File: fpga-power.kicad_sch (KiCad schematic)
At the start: 100 parts, among them U3002 XC7K160T-FFG676

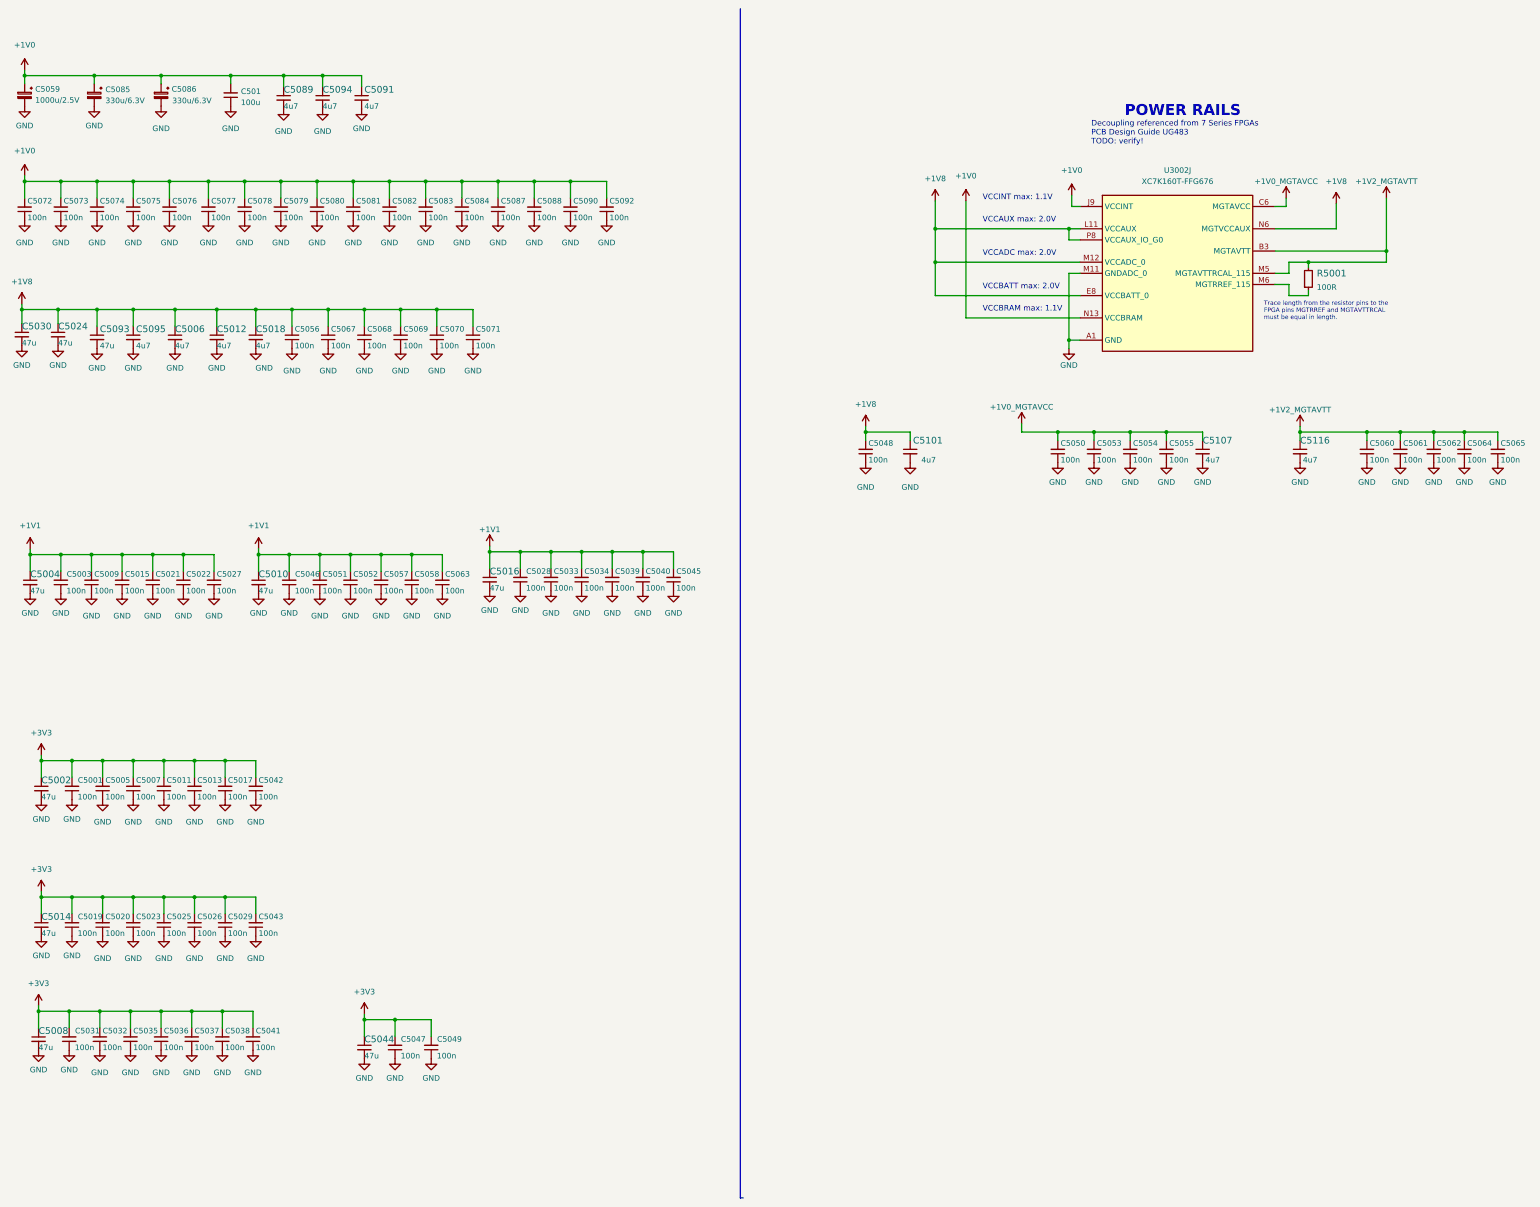
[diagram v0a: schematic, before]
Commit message: Re-annotate schematic
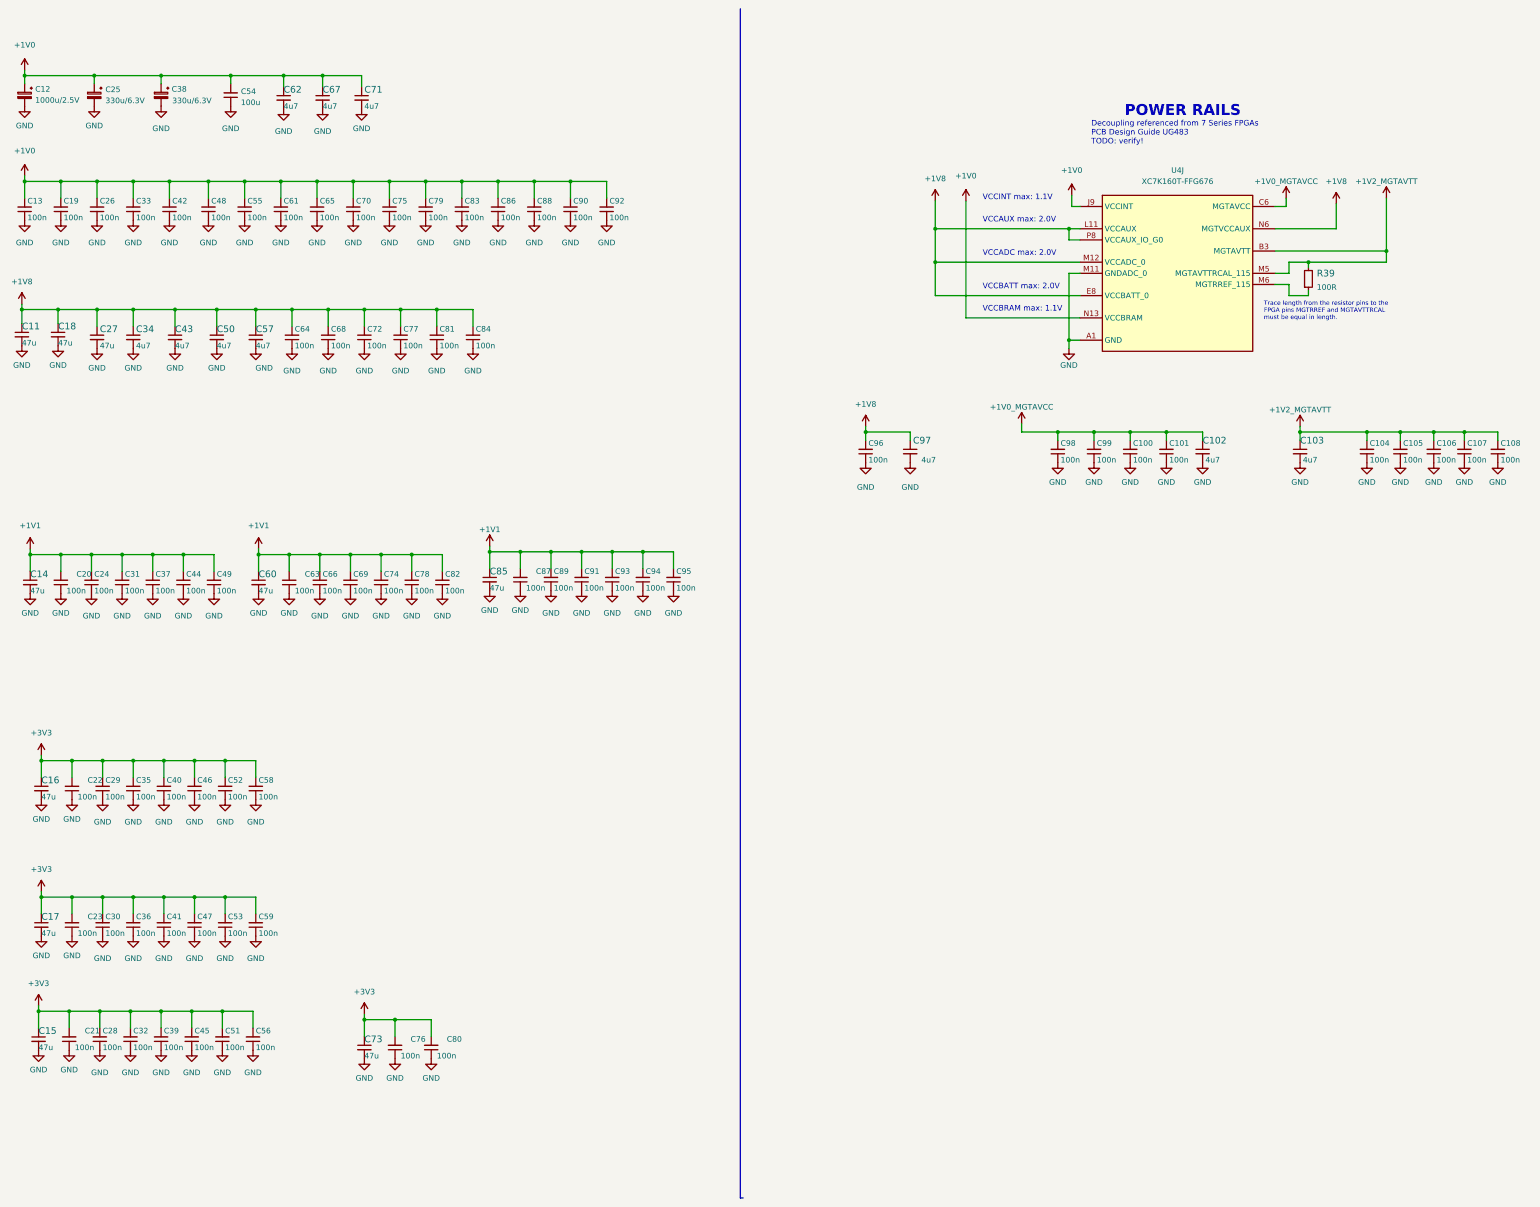
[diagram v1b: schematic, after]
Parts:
- renumbered C5054 to C100, C5055 to C101, C5107 to C102, C5116 to C103, C5060 to C104, C5061 to C105, C5062 to C106, C5064 to C107, C5065 to C108, C5030 to C11, C5059 to C12, C5072 to C13, C5004 to C14, C5008 to C15, C5002 to C16, C5014 to C17, C5024 to C18, C5073 to C19, C5003 to C20, C5031 to C21, C5001 to C22, C5019 to C23, C5009 to C24, C5085 to C25, C5074 to C26, C5093 to C27, C5032 to C28, C5005 to C29, C5020 to C30, C5015 to C31, C5035 to C32, C5075 to C33, C5095 to C34, C5007 to C35, C5023 to C36, C5021 to C37, C5086 to C38, C5036 to C39, C5011 to C40, C5025 to C41, C5076 to C42, C5006 to C43, C5022 to C44, C5037 to C45, C5013 to C46, C5026 to C47, C5077 to C48, C5027 to C49, C5012 to C50, C5038 to C51, C5017 to C52, C5029 to C53, C501 to C54, C5078 to C55, C5041 to C56, C5018 to C57, C5042 to C58, C5043 to C59, C5010 to C60, C5079 to C61, C5089 to C62, C5046 to C63, C5056 to C64, C5080 to C65, C5051 to C66, C5094 to C67, C5067 to C68, C5052 to C69, C5081 to C70, C5091 to C71, C5068 to C72, C5044 to C73, C5057 to C74, C5082 to C75, C5047 to C76, C5069 to C77, C5058 to C78, C5083 to C79, C5049 to C80, C5070 to C81, C5063 to C82, C5084 to C83, C5071 to C84, C5016 to C85, C5087 to C86, C5028 to C87, C5088 to C88, C5033 to C89, C5090 to C90, C5034 to C91, C5092 to C92, C5039 to C93, C5040 to C94, C5045 to C95, C5048 to C96, C5101 to C97, C5050 to C98, C5053 to C99, R5001 to R39, U3002 to U4

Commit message: Add local libraries
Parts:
- C12: footprint antmicro-footprints:C_Pol_EIA-D -> sodimm-ddr5-tester-footprints:C_Pol_EIA-D; symbol antmicroCapacitorspol:C_Pol_1m_2.5V_KEMET-T520-D -> sodimm-ddr5-tester:C_Pol_1m_2.5V_KEMET-T520-D
- C25, C38: footprint antmicro-footprints:C_Pol_EIA-B -> sodimm-ddr5-tester-footprints:C_Pol_EIA-B; symbol antmicroCapacitorspol:C_Pol_330u_6.3V_KEMET-T520-B -> sodimm-ddr5-tester:C_Pol_330u_6.3V_KEMET-T520-B

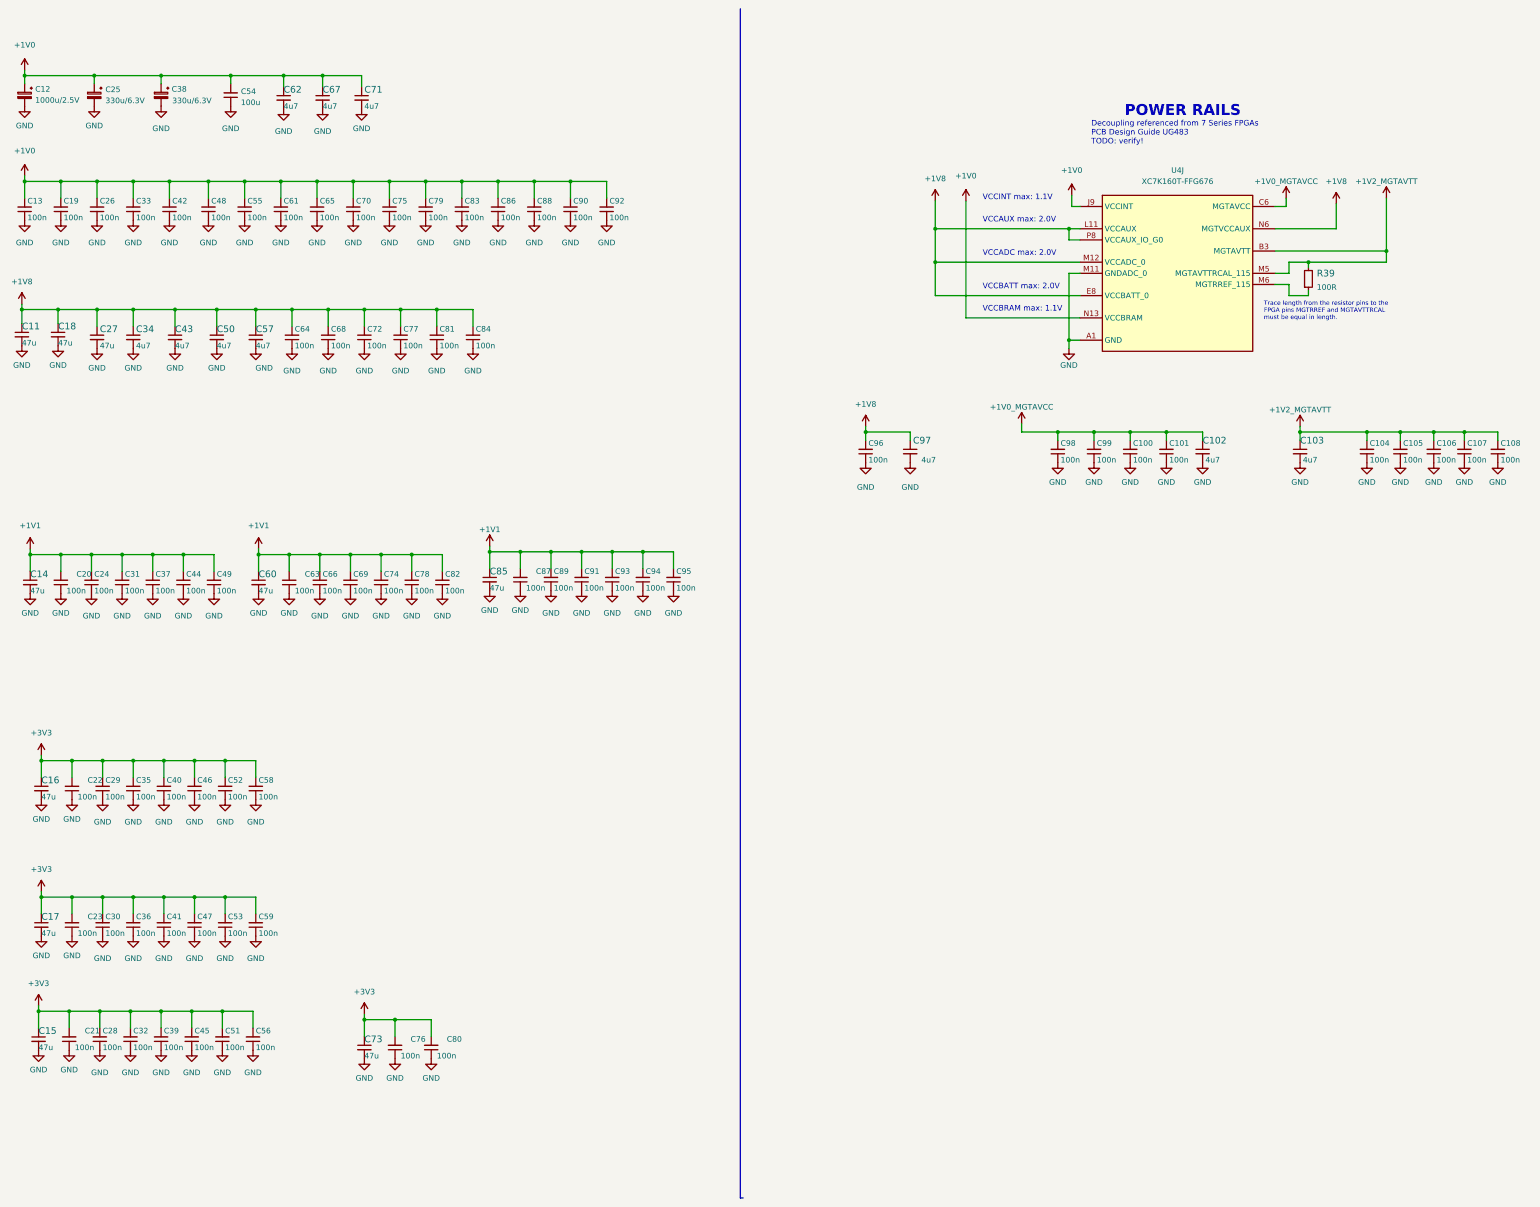
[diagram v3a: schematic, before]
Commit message: Connect DDR hierarchical labels. Define and connect JTAG, RGMII, TDMS, UART, and SDIO buses. Reorganize schematic blocks between sheets
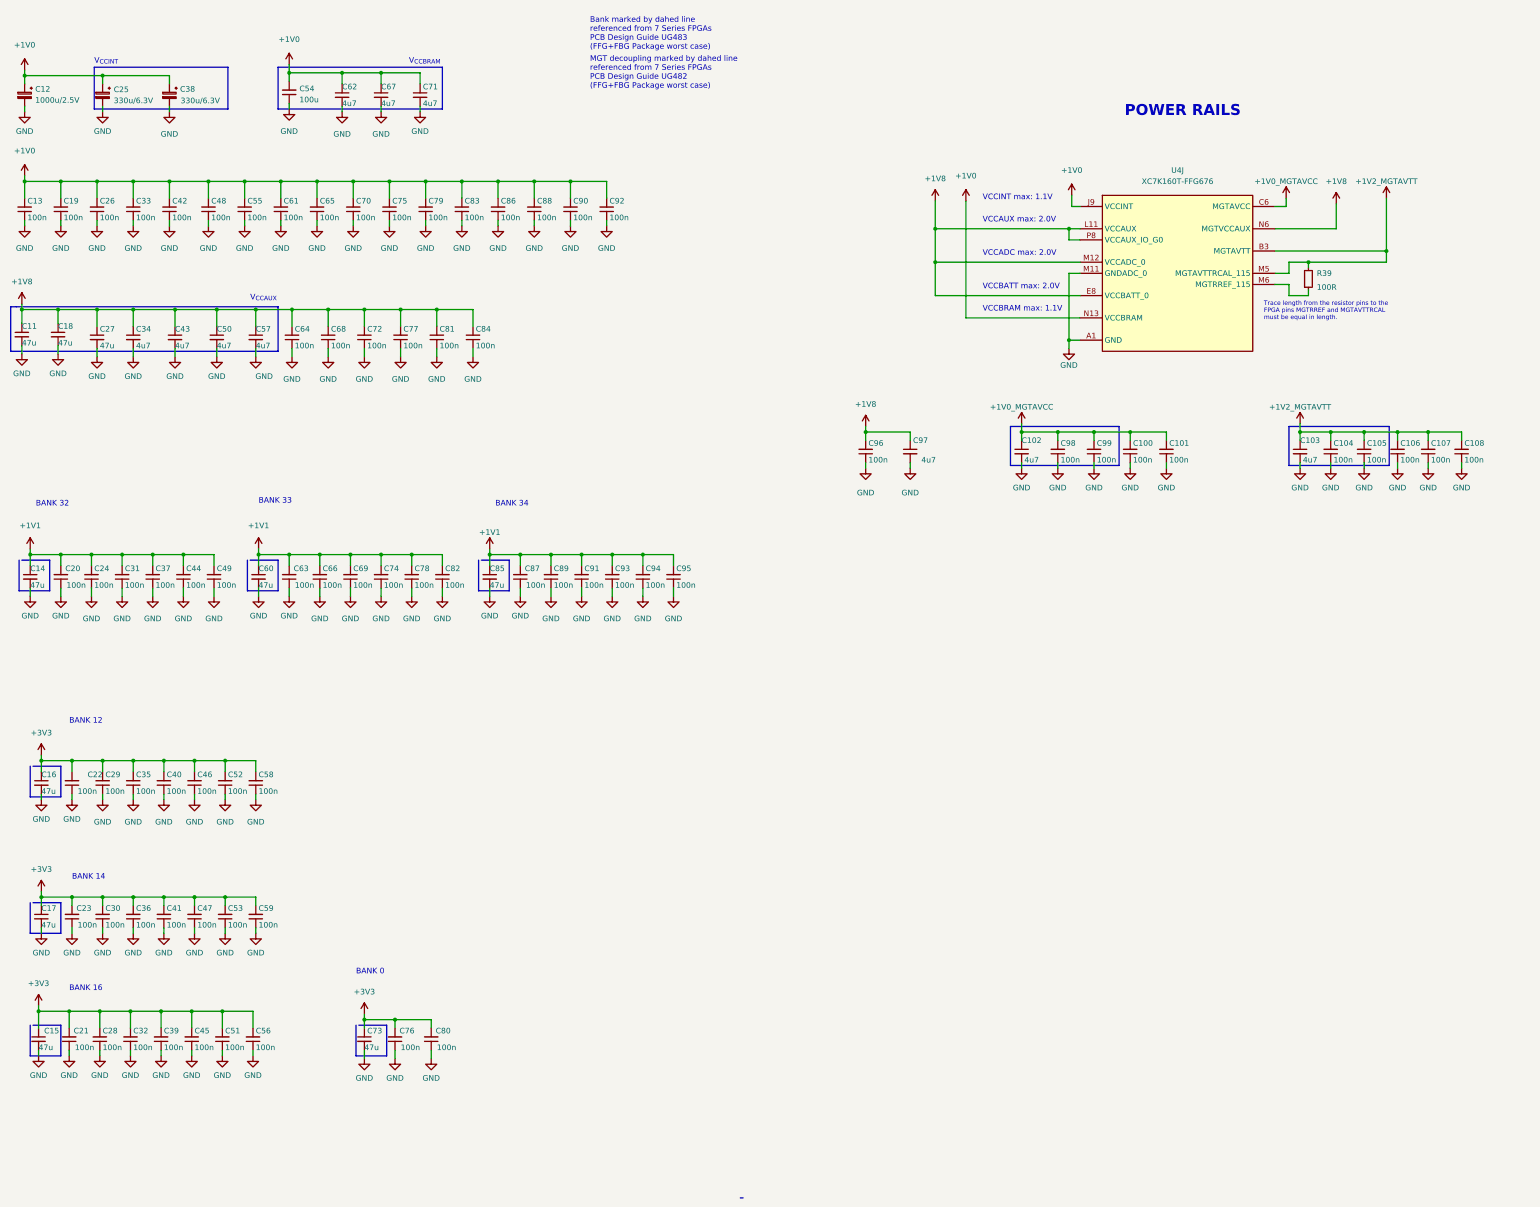
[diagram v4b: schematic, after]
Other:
- note added: "BANK 0"
- note added: "BANK 12"
- note added: "BANK 14"
- note added: "BANK 16"
- note added: "BANK 32"
- note added: "BANK 33"
- note added: "BANK 34"
- note added: "Bank marked by dahed line referenced from 7 Series FPGAs PCB Design Guide UG483 (FFG+FBG Package worst case)"
- note added: "MGT decoupling marked by dahed line referenced from 7 Series FPGAs PCB Design Guide UG482 (FFG+FBG Package worst case)"
- note added: "V_{CCAUX}"
- note added: "V_{CCBRAM}"
- note added: "V_{CCINT}"
- note removed: "Decoupling referenced from 7 Series FPGAs PCB Design Guide UG483 TODO: verify!"
- moved on the sheet: C102, C104, C105, C106, C107, C108, C14, C16, C17, C20, C22, C23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

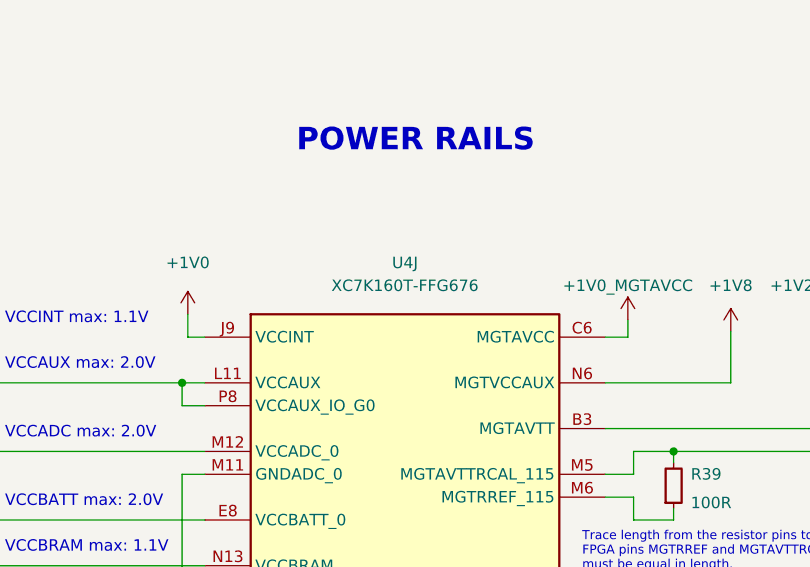
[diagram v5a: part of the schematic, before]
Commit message: Fix FPGA properties from the standardized library, update SO-DIMM symbol
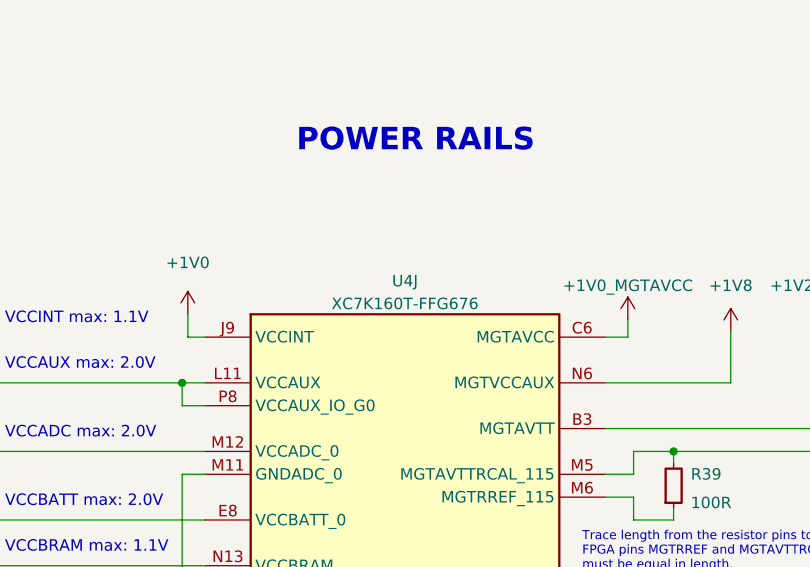
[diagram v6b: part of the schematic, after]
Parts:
- U4: footprint sodimm-ddr5-tester-footprints:BGA-676_27x27mm_Layout26x26_P1X1mm -> antmicro-footprints:BGA-676_27x27mm_Layout26x26_P1X1mm; symbol sodimm-ddr5-tester:XC7K160T-FFG676 -> antmicroMicrocontrollers:XC7K160T-FFG676; Manufacturer Xilinx -> AMD-Xilinx
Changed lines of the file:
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@@
     (pin "1")
   )
-  (symbol (lib_id "sodimm-ddr5-tester:XC7K160T-FFG676") (at 268.605 57.785 0) (unit 10)
+  (symbol (lib_id "antmicroMicrocontrollers:XC7K160T-FFG676") (at 268.605 57.785 0) (unit 10)
     (in_bom yes) (on_board yes) (fields_autoplaced)
-    (property "Reference" "U4" (id 0) (at 290.83 49.53 0))
-    (property "Value" "XC7K160T-FFG676" (id 1) (at 290.83 52.07 0)
+    (property "Reference" "U4" (id 0) (at 290.83 51.5534 0))
+    (property "Value" "XC7K160T-FFG676" (id 1) (at 290.83 54.0837 0)
       (effects (font (size 1.27 1.27) (thickness 0.15)))
     )
-    (property "Footprint" "sodimm-ddr5-tester-footprints:BGA-676_27x27mm_Layout26x26_P1X1mm" (id 2) (at 337.185 60.325 0)
+    (property "Footprint" "antmicro-footprints:BGA-676_27x27mm_Layout26x26_P1X1mm" (id 2) (at 337.185 60.325 0)
       (effects (font (size 1.27 1.27) (thickness 0.15)) (justify left bottom) hide)
     )
@@
       (effects (font (size 1.27 1.27) (thickness 0.15)) (justify left bottom) hide)
     )
-    (property "Manufacturer" "Xilinx" (id 7) (at 268.605 57.785 0)
+    (property "Manufacturer" "AMD-Xilinx" (id 7) (at 268.605 57.785 0)
       (effects (font (size 1.27 1.27)) hide)
     )

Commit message: Loclib of the project
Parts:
- U4: footprint antmicro-footprints:BGA-676_27x27mm_Layout26x26_P1X1mm -> sodimm-ddr5-tester-footprints:BGA-676_27x27mm_Layout26x26_P1X1mm; symbol antmicroMicrocontrollers:XC7K160T-FFG676 -> sodimm-ddr5-tester:XC7K160T-FFG676
